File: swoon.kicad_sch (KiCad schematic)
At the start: 151 parts, among them J1 3305-0-15-80-47-27-10-0, J10 3305-0-15-80-47-27-10-0, J11 3305-0-15-80-47-27-10-0, J12 3305-0-15-80-47-27-10-0, J13 3305-0-15-80-47-27-10-0, J14 3305-0-15-80-47-27-10-0, J15 3305-0-15-80-47-27-10-0, J16 3305-0-15-80-47-27-10-0, J17 3305-0-15-80-47-27-10-0, J18 3305-0-15-80-47-27-10-0, J19 3305-0-15-80-47-27-10-0, J2 3305-0-15-80-47-27-10-0, J20 3305-0-15-80-47-27-10-0, J21 3305-0-15-80-47-27-10-0, J22 3305-0-15-80-47-27-10-0, J23 3305-0-15-80-47-27-10-0, J24 3305-0-15-80-47-27-10-0, J25 3305-0-15-80-47-27-10-0, J26 3305-0-15-80-47-27-10-0, J27 3305-0-15-80-47-27-10-0, J28 3305-0-15-80-47-27-10-0, J29 3305-0-15-80-47-27-10-0, J3 3305-0-15-80-47-27-10-0, J30 3305-0-15-80-47-27-10-0, J31 3305-0-15-80-47-27-10-0, J32 3305-0-15-80-47-27-10-0, J33 3305-0-15-80-47-27-10-0, J34 3305-0-15-80-47-27-10-0, J35 3305-0-15-80-47-27-10-0, J36 3305-0-15-80-47-27-10-0, J37 3305-0-15-80-47-27-10-0, J38 3305-0-15-80-47-27-10-0, J39 3305-0-15-80-47-27-10-0, J4 3305-0-15-80-47-27-10-0, J40 3305-0-15-80-47-27-10-0, J41 3305-0-15-80-47-27-10-0, J42 3305-0-15-80-47-27-10-0, J43 3305-0-15-80-47-27-10-0, J44 3305-0-15-80-47-27-10-0, J45 3305-0-15-80-47-27-10-0, J46 3305-0-15-80-47-27-10-0, J47 3305-0-15-80-47-27-10-0, J48 3305-0-15-80-47-27-10-0, J49 3305-0-15-80-47-27-10-0, J5 3305-0-15-80-47-27-10-0, J50 3305-0-15-80-47-27-10-0, J51 3305-0-15-80-47-27-10-0, J52 3305-0-15-80-47-27-10-0, J53 3305-0-15-80-47-27-10-0, J54 3305-0-15-80-47-27-10-0, J55 3305-0-15-80-47-27-10-0, J56 3305-0-15-80-47-27-10-0, J57 3305-0-15-80-47-27-10-0, J58 3305-0-15-80-47-27-10-0, J59 3305-0-15-80-47-27-10-0, J6 3305-0-15-80-47-27-10-0, J60 3305-0-15-80-47-27-10-0, J61 3305-0-15-80-47-27-10-0, J62 3305-0-15-80-47-27-10-0, J63 3305-0-15-80-47-27-10-0, J64 3305-0-15-80-47-27-10-0, J65 3305-0-15-80-47-27-10-0, J66 3305-0-15-80-47-27-10-0, J67 3305-0-15-80-47-27-10-0, J68 3305-0-15-80-47-27-10-0, J69 310-13-107-41-001000, J7 3305-0-15-80-47-27-10-0, J70 310-13-107-41-001000, J71 310-13-107-41-001000, J72 310-13-107-41-001000, J73 Mill Max 0906-2-15-20-75-14-1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, J74 Mill Max 0906-2-15-20-75-14-1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, J8 3305-0-15-80-47-27-10-0, J9 3305-0-15-80-47-27-10-0, SW1 SW_Push, SW10 SW_Push, SW11 SW_Push, SW12 SW_Push, SW13 SW_Push, SW14 SW_Push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

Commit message: add devcontainer
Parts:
- H1, U1: now left out of the parts list
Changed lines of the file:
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@@
 		(unit 1)
 		(exclude_from_sim no)
-		(in_bom yes)
+		(in_bom no)
 		(on_board yes)
 		(dnp no)
@@
 		(unit 1)
 		(exclude_from_sim no)
-		(in_bom yes)
-		(on_board yes)
-		(dnp no)
+		(in_bom no)
+		(on_board yes)
+		(dnp no)

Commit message: organize devcontainer
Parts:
- J1, J10, J13, J14, J17, J18, J2, J21, J22, J25, J26, J29, J30, J33, J34, J37, J38, J41, J42, J45, J46, J49, J5, J50, J53, J54, J57, J58, J6, J61, J62, J65, J66, J69, J71, J73, J9: Config +left,+flip -> +left
- J11, J12, J15, J16, J19, J20, J23, J24, J27, J28, J3, J31, J32, J35, J36, J39, J4, J40, J43, J44, J47, J48, J51, J52, J55, J56, J59, J60, J63, J64, J67, J68, J7, J70, J72, J74, J8: Config +right,+flip -> +right
- TP1, TP15, TP17, TP5, TP9: Config +right -> +left
- TP10, TP16, TP18, TP2, TP6: Config +left -> +right

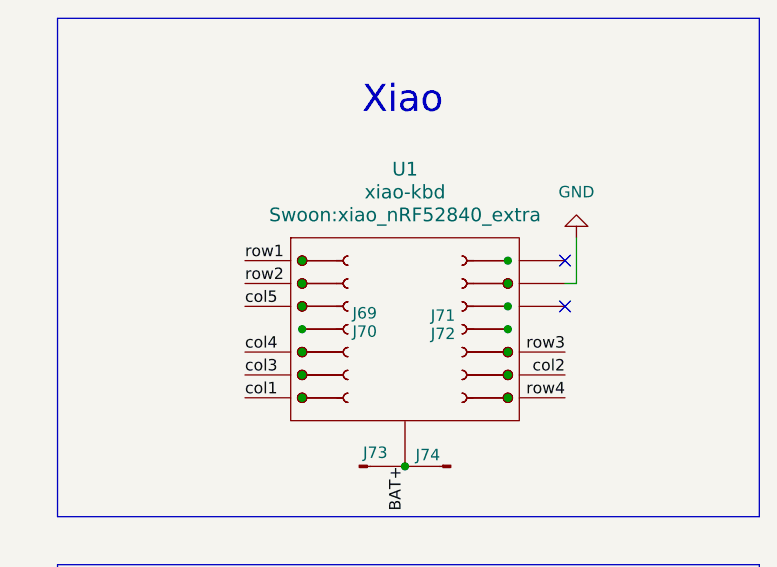
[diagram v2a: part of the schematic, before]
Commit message: fix testpads, update kibot.yaml
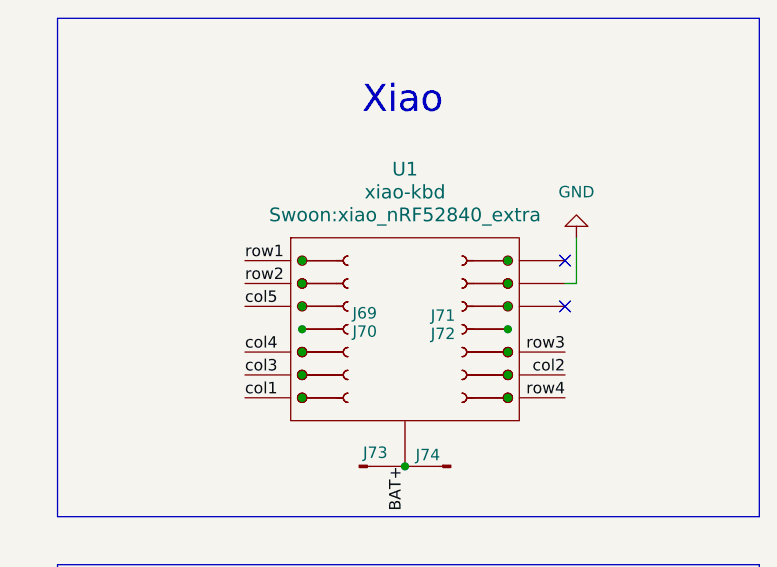
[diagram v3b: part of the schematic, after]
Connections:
- net at J69.1 (Pin_1), J70.1 (Pin_1), TP1.1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: no longer TP2.1
- net at J69.2 (Pin_2), J70.2 (Pin_2), TP3.1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: now also TP20.1; no longer TP4.1
- net at J69.3 (Pin_3), J70.3 (Pin_3), TP5.1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: no longer TP6.1
- net at J69.5 (Pin_5), J70.5 (Pin_5), TP7.1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: now also TP14.1; no longer TP8.1
- net at J69.6 (Pin_6), J70.6 (Pin_6), TP9.1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: now also TP16.1; no longer TP10.1
- net at J69.7 (Pin_7), J70.7 (Pin_7), TP11.1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: now also TP18.1; no longer TP12.1
- net at J71.5 (Pin_5), J72.5 (Pin_5), TP13.1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: now also TP8.1; no longer TP14.1
- net at J71.2 (Pin_2), J72.2 (Pin_2), TP19.1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: now also TP4.1; no longer TP20.1
- net at J71.1 (Pin_1), J72.1 (Pin_1), U1.29 (hole): now also TP2.1
- net at J71.3 (Pin_3), J72.3 (Pin_3), U1.27 (hole): now also TP6.1
- net at J71.6 (Pin_6), J72.6 (Pin_6), TP15.1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: now also TP10.1; no longer TP16.1
- net at J71.7 (Pin_7), J72.7 (Pin_7), TP17.1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: now also TP12.1; no longer TP18.1

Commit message: erroring var_rename stuff
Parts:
- D1, D10, D11, D12, D13, D14, D15, D16, D17, D18, D19, D2, D20, D21, D22, D23, D24, D25, D26, D27, D28, D29, D3, D30, D31, D32, D33, D34, D4, D5, D6, D7, D8, D9: left:Footprint (none) -> Swoon:D_0805_2012Metric; right:Footprint (none) -> Swoon:D_0805_2012Metric
- H1: left:Footprint (none) -> Swoon:Tenting_Puck2; right:Footprint (none) -> Swoon:Tenting_Puck2
- J1, J10, J13, J14, J17, J18, J2, J21, J22, J25, J26, J29, J30, J33, J34, J37, J38, J41, J42, J45, J46, J49, J5, J50, J53, J54, J57, J58, J6, J61, J62, J65, J66, J9: footprint Swoon:3305-0-15-80-47-27-10-0 -> Swoon:TestPoint_Pad_Empty; left:Footprint (none) -> Swoon:3305-0-15-80-47-27-10-0; right:Footprint (none) -> Swoon:TestPoint_Pad_Empty
- J11, J12, J15, J16, J19, J20, J23, J24, J27, J28, J3, J31, J32, J35, J36, J39, J4, J40, J43, J44, J47, J48, J51, J52, J55, J56, J59, J60, J63, J64, J67, J68, J7, J8: footprint Swoon:3305-0-15-80-47-27-10-0 -> Swoon:TestPoint_Pad_Empty; left:Footprint (none) -> Swoon:TestPoint_Pad_Empty; right:Footprint (none) -> Swoon:3305-0-15-80-47-27-10-0
- J69, J70, J71, J72: left:Footprint (none) -> Swoon:MF254V-11-07-0743; right:Footprint (none) -> Swoon:MF254V-11-07-0743
- J73: footprint Swoon:0906-2-15-20-75-14-11-0 -> Swoon:TestPoint_Pad_Empty; left:Footprint (none) -> Swoon:0906-2-15-20-75-14-11-0; right:Footprint (none) -> Swoon:TestPoint_Pad_Empty
- J74: footprint Swoon:0906-2-15-20-75-14-11-0 -> Swoon:TestPoint_Pad_Empty; left:Footprint (none) -> Swoon:TestPoint_Pad_Empty; right:Footprint (none) -> Swoon:0906-2-15-20-75-14-11-0
- SW1, SW10, SW11, SW12, SW13, SW14, SW15, SW16, SW17, SW2, SW3, SW4, SW5, SW6, SW7, SW8, SW9: left:Footprint (none) -> Swoon:SW_PG1350_vias; right:Footprint (none) -> Swoon:SW_PG1350_vias
- SW18, SW19: left:Footprint (none) -> Swoon:SW-SMD_MST22D18G2; right:Footprint (none) -> Swoon:SW-SMD_MST22D18G2
- TP1, TP11, TP13, TP15, TP17, TP19, TP3, TP5, TP7, TP9: footprint TestPoint:TestPoint_Pad_1.0x1.0mm -> Swoon:TestPoint_Pad_Empty; left:Footprint (none) -> TestPoint:TestPoint_Pad_1.0x1.0mm; right:Footprint (none) -> Swoon:TestPoint_Pad_Empty
- TP10, TP12, TP14, TP16, TP18, TP2, TP20, TP4, TP6, TP8: footprint TestPoint:TestPoint_Pad_1.0x1.0mm -> Swoon:TestPoint_Pad_Empty; left:Footprint (none) -> Swoon:TestPoint_Pad_Empty; right:Footprint (none) -> TestPoint:TestPoint_Pad_1.0x1.0mm
- U1: left:Footprint (none) -> Swoon:xiao_nRF52840_extra; right:Footprint (none) -> Swoon:xiao_nRF52840_extra
- U2, U3: left:Footprint (none) -> Swoon:BAT-SMD_MY-LR44-02; right:Footprint (none) -> Swoon:BAT-SMD_MY-LR44-02

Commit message: fix 3d models
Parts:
- D1, D11, D13, D15, D17, D19, D21, D23, D25, D27, D29, D3, D31, D33, D5, D7, D9: right:Footprint Swoon:D_0805_2012Metric -> (none)
- D10, D12, D14, D16, D18, D2, D20, D22, D24, D26, D28, D30, D32, D34, D4, D6, D8: left:Footprint Swoon:D_0805_2012Metric -> (none)
- J1, J10, J13, J14, J17, J18, J2, J21, J22, J25, J26, J29, J30, J33, J34, J37, J38, J41, J42, J45, J46, J49, J5, J50, J53, J54, J57, J58, J6, J61, J62, J65, J66, J73, J9, TP1, TP11, TP13, TP15, TP17, TP19, TP3, TP5, TP7, TP9: right:Footprint Swoon:TestPoint_Pad_Empty -> (none)
- J11, J12, J15, J16, J19, J20, J23, J24, J27, J28, J3, J31, J32, J35, J36, J39, J4, J40, J43, J44, J47, J48, J51, J52, J55, J56, J59, J60, J63, J64, J67, J68, J7, J74, J8, TP10, TP12, TP14, TP16, TP18, TP2, TP20, TP4, TP6, TP8: left:Footprint Swoon:TestPoint_Pad_Empty -> (none)
- J69, J71: right:Footprint Swoon:MF254V-11-07-0743 -> (none)
- J70, J72: left:Footprint Swoon:MF254V-11-07-0743 -> (none)
- SW18: right:Footprint Swoon:SW-SMD_MST22D18G2 -> (none)
- SW19: left:Footprint Swoon:SW-SMD_MST22D18G2 -> (none)
- U2: right:Footprint Swoon:BAT-SMD_MY-LR44-02 -> (none)
- U3: left:Footprint Swoon:BAT-SMD_MY-LR44-02 -> (none)

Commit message: clean up
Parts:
- D1, D11, D13, D15, D17, D19, D21, D23, D25, D27, D29, D3, D31, D33, D5, D7, D9, J1, J10, J13, J14, J17, J18, J2, J21, J22, J25, J26, J29, J30, J33, J34, J37, J38, J41, J42, J45, J46, J49, J5, J50, J53, J54, J57, J58, J6, J61, J62, J65, J66, J69, J71, J73, J9, SW18, TP1, TP11, TP13, TP15, TP17, TP19, TP3, TP5, TP7, TP9, U2: right:Footprint (none) -> Swoon:TestPoint_Pad_Empty
- D10, D12, D14, D16, D18, D2, D20, D22, D24, D26, D28, D30, D32, D34, D4, D6, D8, J11, J12, J15, J16, J19, J20, J23, J24, J27, J28, J3, J31, J32, J35, J36, J39, J4, J40, J43, J44, J47, J48, J51, J52, J55, J56, J59, J60, J63, J64, J67, J68, J7, J70, J72, J74, J8, SW19, TP10, TP12, TP14, TP16, TP18, TP2, TP20, TP4, TP6, TP8, U3: left:Footprint (none) -> Swoon:TestPoint_Pad_Empty

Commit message: add zips of Flip, Left, and Right variants
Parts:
- D1, D10, D11, D12, D13, D14, D15, D16, D17, D18, D19, D2, D20, D21, D22, D23, D24, D25, D26, D27, D28, D29, D3, D30, D31, D32, D33, D34, D4, D5, D6, D7, D8, D9: flip:Footprint (none) -> Swoon:D_0805_2012Metric
- H1: flip:Footprint (none) -> Swoon:Tenting_Puck2
- J1, J10, J11, J12, J13, J14, J15, J16, J17, J18, J19, J2, J20, J21, J22, J23, J24, J25, J26, J27, J28, J29, J3, J30, J31, J32, J33, J34, J35, J36, J37, J38, J39, J4, J40, J41, J42, J43, J44, J45, J46, J47, J48, J49, J5, J50, J51, J52, J53, J54, J55, J56, J57, J58, J59, J6, J60, J61, J62, J63, J64, J65, J66, J67, J68, J7, J8, J9: footprint Swoon:TestPoint_Pad_Empty -> Swoon:3305-0-15-80-47-27-10-0; flip:Footprint (none) -> Swoon:TestPoint_Pad_Empty
- J69, J70, J71, J72: flip:Footprint (none) -> Swoon:TestPoint_Pad_Empty
- J73, J74: footprint Swoon:TestPoint_Pad_Empty -> Swoon:0906-2-15-20-75-14-11-0; flip:Footprint (none) -> Swoon:TestPoint_Pad_Empty
- SW1, SW10, SW11, SW12, SW13, SW14, SW15, SW16, SW17, SW2, SW3, SW4, SW5, SW6, SW7, SW8, SW9: flip:Footprint (none) -> Swoon:SW_PG1350_vias
- SW18, SW19: flip:Footprint (none) -> Swoon:SW-SMD_MST22D18G2
- TP1, TP11, TP13, TP15, TP17, TP19, TP3, TP5, TP7, TP9: footprint Swoon:TestPoint_Pad_Empty -> Swoon:TestPoint_Pad_1.0x1.0mm; flip:Footprint (none) -> Swoon:TestPoint_Pad_Empty; left:Footprint TestPoint:TestPoint_Pad_1.0x1.0mm -> Swoon:TestPoint_Pad_1.0x1.0mm
- TP10, TP12, TP14, TP16, TP18, TP2, TP20, TP4, TP6, TP8: footprint Swoon:TestPoint_Pad_Empty -> Swoon:TestPoint_Pad_1.0x1.0mm; flip:Footprint (none) -> Swoon:TestPoint_Pad_Empty; right:Footprint TestPoint:TestPoint_Pad_1.0x1.0mm -> Swoon:TestPoint_Pad_1.0x1.0mm
- U1: flip:Footprint (none) -> Swoon:xiao_nRF52840_extra
- U2, U3: flip:Footprint (none) -> Swoon:BAT-SMD_MY-LR44-02

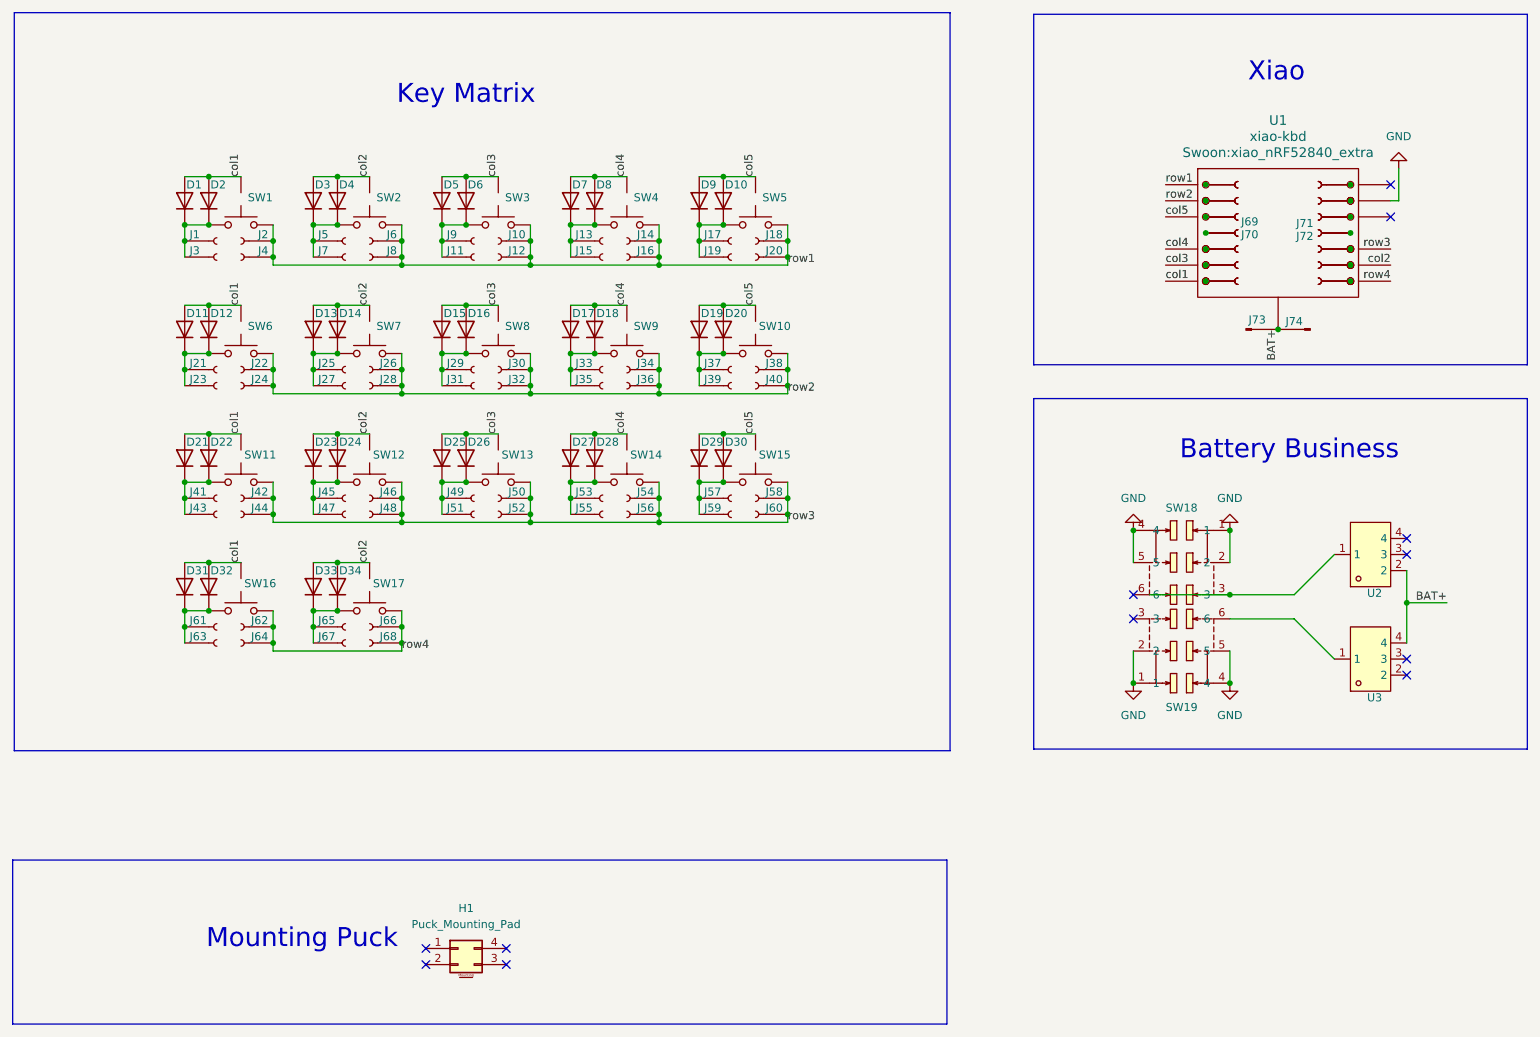
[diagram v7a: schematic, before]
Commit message: reroute switches
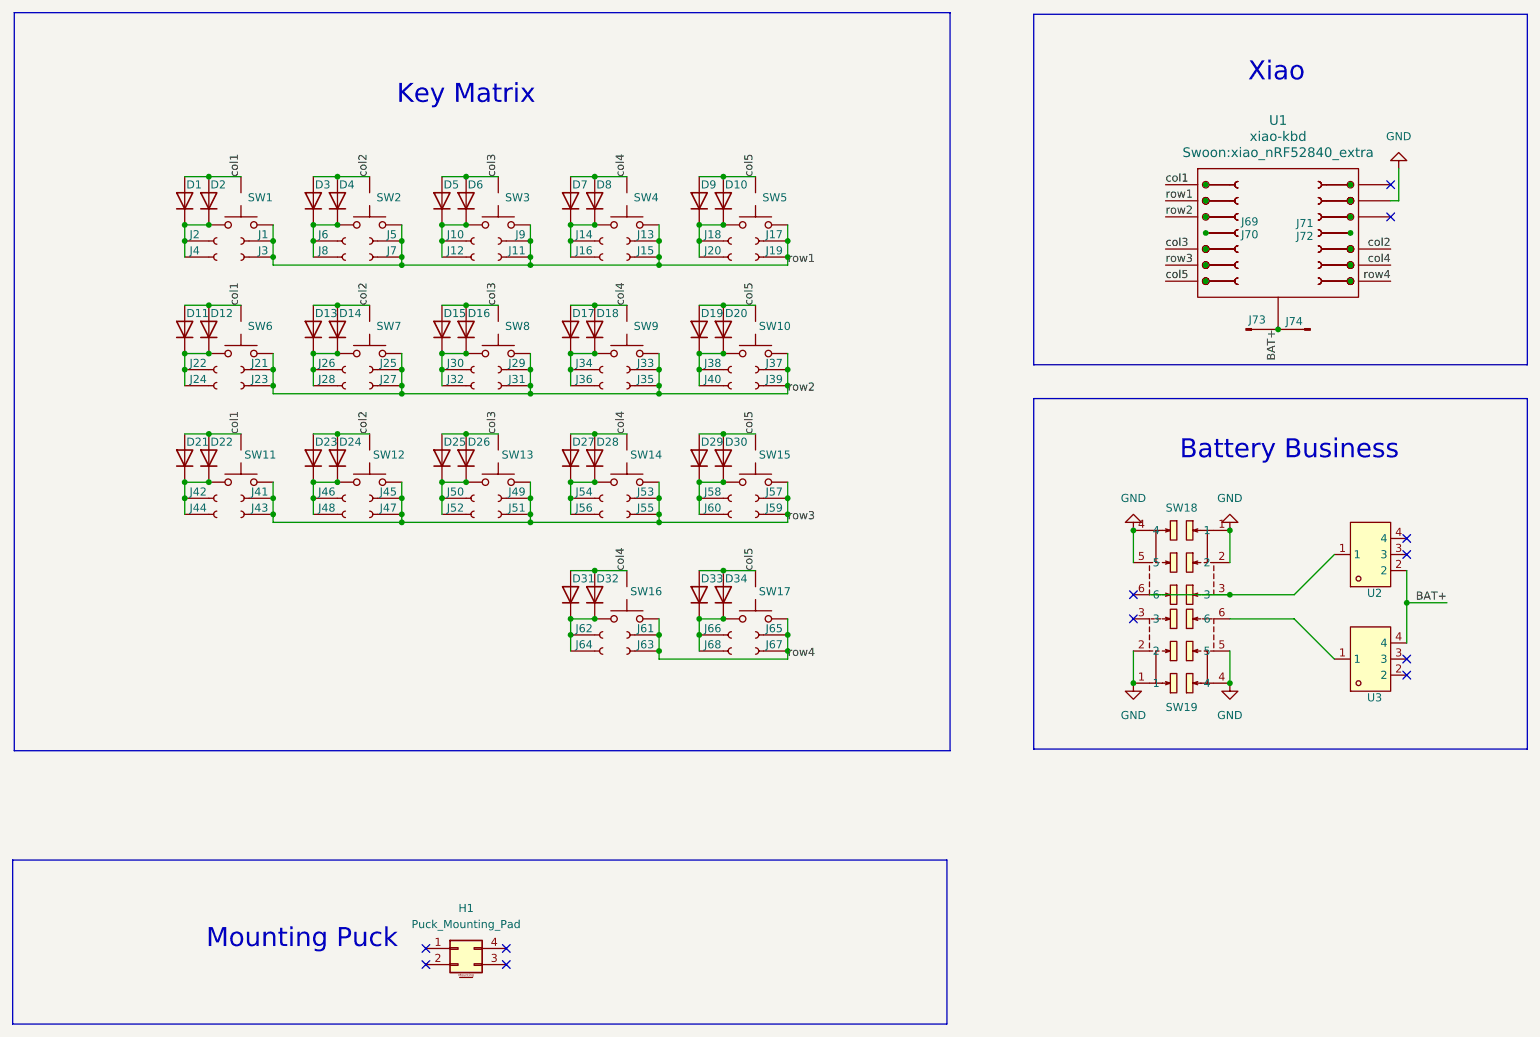
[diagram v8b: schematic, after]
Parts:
- TP1, TP10, TP11, TP12, TP13, TP14, TP15, TP16, TP17, TP18, TP19, TP2, TP20, TP3, TP4, TP5, TP6, TP7, TP8, TP9: footprint Swoon:TestPoint_Pad_1.0x1.0mm -> Swoon:TestPoint_Pad_Empty
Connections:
- net col1: now also U1.1 (D0); no longer D31.2 (A), D32.2 (A), SW16.3, U1.7 (D6)
- net col2: now also U1.10 (D9); no longer D33.2 (A), D34.2 (A), SW17.3, U1.9 (D8)
- net col3: now also U1.5 (D4); no longer U1.6 (D5)
- net col4: now also D31.2 (A), D32.2 (A), SW16.3, U1.9 (D8); no longer U1.5 (D4)
- net col5: now also D33.2 (A), D34.2 (A), SW17.3, U1.7 (D6); no longer U1.3 (D2)
- net row1: now also J1.1 (Pin_1), J11.1 (Pin_1), J13.1 (Pin_1), J15.1 (Pin_1), J17.1 (Pin_1), J19.1 (Pin_1), J3.1 (Pin_1), J5.1 (Pin_1), J7.1 (Pin_1), J9.1 (Pin_1), U1.2 (D1); no longer J10.1 (Pin_1), J12.1 (Pin_1), J14.1 (Pin_1), J16.1 (Pin_1), J18.1 (Pin_1), J2.1 (Pin_1), J20.1 (Pin_1), J4.1 (Pin_1), J6.1 (Pin_1), J8.1 (Pin_1), U1.1 (D0)
- net row2: now also J21.1 (Pin_1), J23.1 (Pin_1), J25.1 (Pin_1), J27.1 (Pin_1), J29.1 (Pin_1), J31.1 (Pin_1), J33.1 (Pin_1), J35.1 (Pin_1), J37.1 (Pin_1), J39.1 (Pin_1), U1.3 (D2); no longer J22.1 (Pin_1), J24.1 (Pin_1), J26.1 (Pin_1), J28.1 (Pin_1), J30.1 (Pin_1), J32.1 (Pin_1), J34.1 (Pin_1), J36.1 (Pin_1), J38.1 (Pin_1), J40.1 (Pin_1), U1.2 (D1)
- net row3: now also J41.1 (Pin_1), J43.1 (Pin_1), J45.1 (Pin_1), J47.1 (Pin_1), J49.1 (Pin_1), J51.1 (Pin_1), J53.1 (Pin_1), J55.1 (Pin_1), J57.1 (Pin_1), J59.1 (Pin_1), U1.6 (D5); no longer J42.1 (Pin_1), J44.1 (Pin_1), J46.1 (Pin_1), J48.1 (Pin_1), J50.1 (Pin_1), J52.1 (Pin_1), J54.1 (Pin_1), J56.1 (Pin_1), J58.1 (Pin_1), J60.1 (Pin_1), U1.10 (D9)
- net row4: now also J61.1 (Pin_1), J63.1 (Pin_1), J65.1 (Pin_1), J67.1 (Pin_1); no longer J62.1 (Pin_1), J64.1 (Pin_1), J66.1 (Pin_1), J68.1 (Pin_1)
- net at D31.1 (K), D32.1 (K), SW16.2: now also J62.1 (Pin_1), J64.1 (Pin_1); no longer J61.1 (Pin_1), J63.1 (Pin_1)
- net at D23.1 (K), D24.1 (K), SW12.2: now also J46.1 (Pin_1), J48.1 (Pin_1); no longer J45.1 (Pin_1), J47.1 (Pin_1)
- net at D17.1 (K), D18.1 (K), SW9.2: now also J34.1 (Pin_1), J36.1 (Pin_1); no longer J33.1 (Pin_1), J35.1 (Pin_1)
- net at D33.1 (K), D34.1 (K), SW17.2: now also J66.1 (Pin_1), J68.1 (Pin_1); no longer J65.1 (Pin_1), J67.1 (Pin_1)
- net at D19.1 (K), D20.1 (K), SW10.2: now also J38.1 (Pin_1), J40.1 (Pin_1); no longer J37.1 (Pin_1), J39.1 (Pin_1)
- net at D1.1 (K), D2.1 (K), SW1.2: now also J2.1 (Pin_1), J4.1 (Pin_1); no longer J1.1 (Pin_1), J3.1 (Pin_1)
- net at D15.1 (K), D16.1 (K), SW8.2: now also J30.1 (Pin_1), J32.1 (Pin_1); no longer J29.1 (Pin_1), J31.1 (Pin_1)
- net at D29.1 (K), D30.1 (K), SW15.2: now also J58.1 (Pin_1), J60.1 (Pin_1); no longer J57.1 (Pin_1), J59.1 (Pin_1)
- net at D10.1 (K), D9.1 (K), SW5.2: now also J18.1 (Pin_1), J20.1 (Pin_1); no longer J17.1 (Pin_1), J19.1 (Pin_1)
- net at D5.1 (K), D6.1 (K), SW3.2: now also J10.1 (Pin_1), J12.1 (Pin_1); no longer J11.1 (Pin_1), J9.1 (Pin_1)
- net at D27.1 (K), D28.1 (K), SW14.2: now also J54.1 (Pin_1), J56.1 (Pin_1); no longer J53.1 (Pin_1), J55.1 (Pin_1)
- net at D25.1 (K), D26.1 (K), SW13.2: now also J50.1 (Pin_1), J52.1 (Pin_1); no longer J49.1 (Pin_1), J51.1 (Pin_1)
- net at D13.1 (K), D14.1 (K), SW7.2: now also J26.1 (Pin_1), J28.1 (Pin_1); no longer J25.1 (Pin_1), J27.1 (Pin_1)
- net at D3.1 (K), D4.1 (K), SW2.2: now also J6.1 (Pin_1), J8.1 (Pin_1); no longer J5.1 (Pin_1), J7.1 (Pin_1)
- net at D7.1 (K), D8.1 (K), SW4.2: now also J14.1 (Pin_1), J16.1 (Pin_1); no longer J13.1 (Pin_1), J15.1 (Pin_1)
- net at D21.1 (K), D22.1 (K), SW11.2: now also J42.1 (Pin_1), J44.1 (Pin_1); no longer J41.1 (Pin_1), J43.1 (Pin_1)
- net at D11.1 (K), D12.1 (K), SW6.2: now also J22.1 (Pin_1), J24.1 (Pin_1); no longer J21.1 (Pin_1), J23.1 (Pin_1)
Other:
- moved on the sheet: D31, D32, D33, D34, J1, J10, J11, J12, J13, J14, J15, J16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
